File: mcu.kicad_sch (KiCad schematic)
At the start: 5 parts, among them J3 USB_C_Receptacle_USB2.0_16P, M1 Module-stlink-0.1, M3 Module-mega-mcu144-0.6

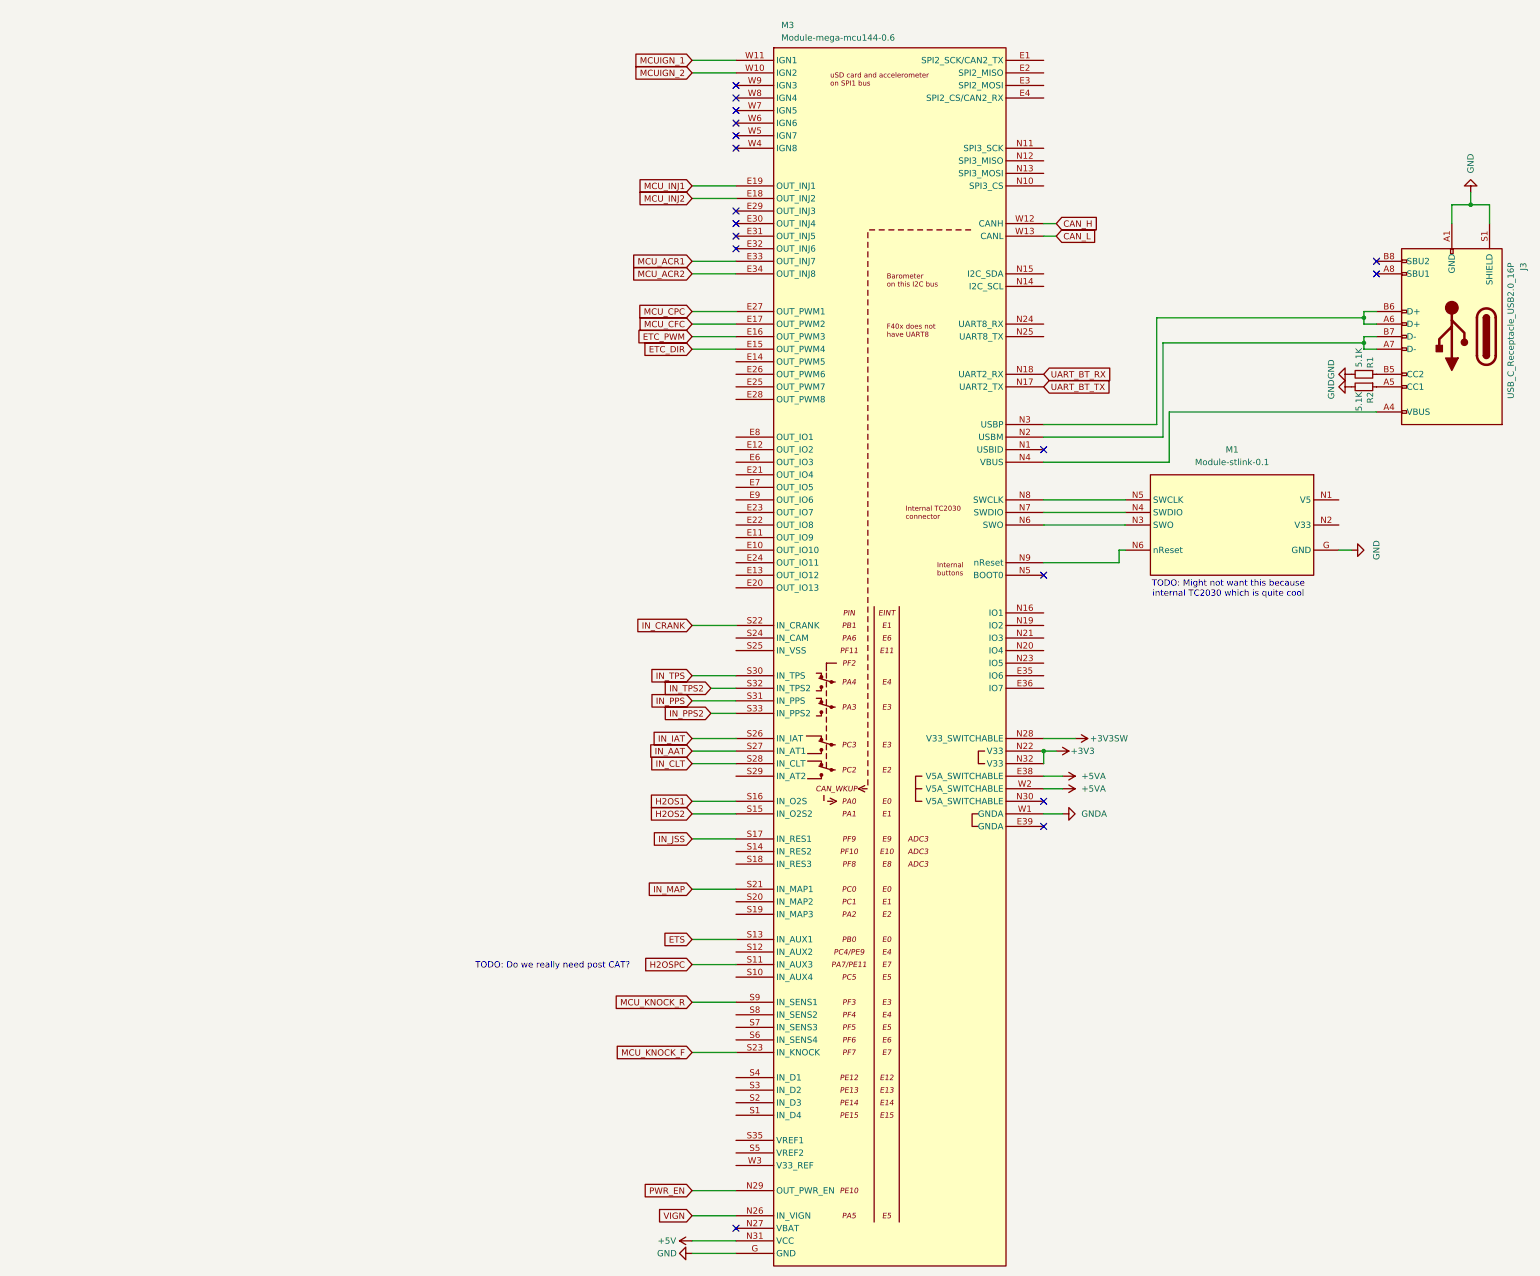
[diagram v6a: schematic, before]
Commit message: adding most remaining outputs and sensors like vvt, cam etc
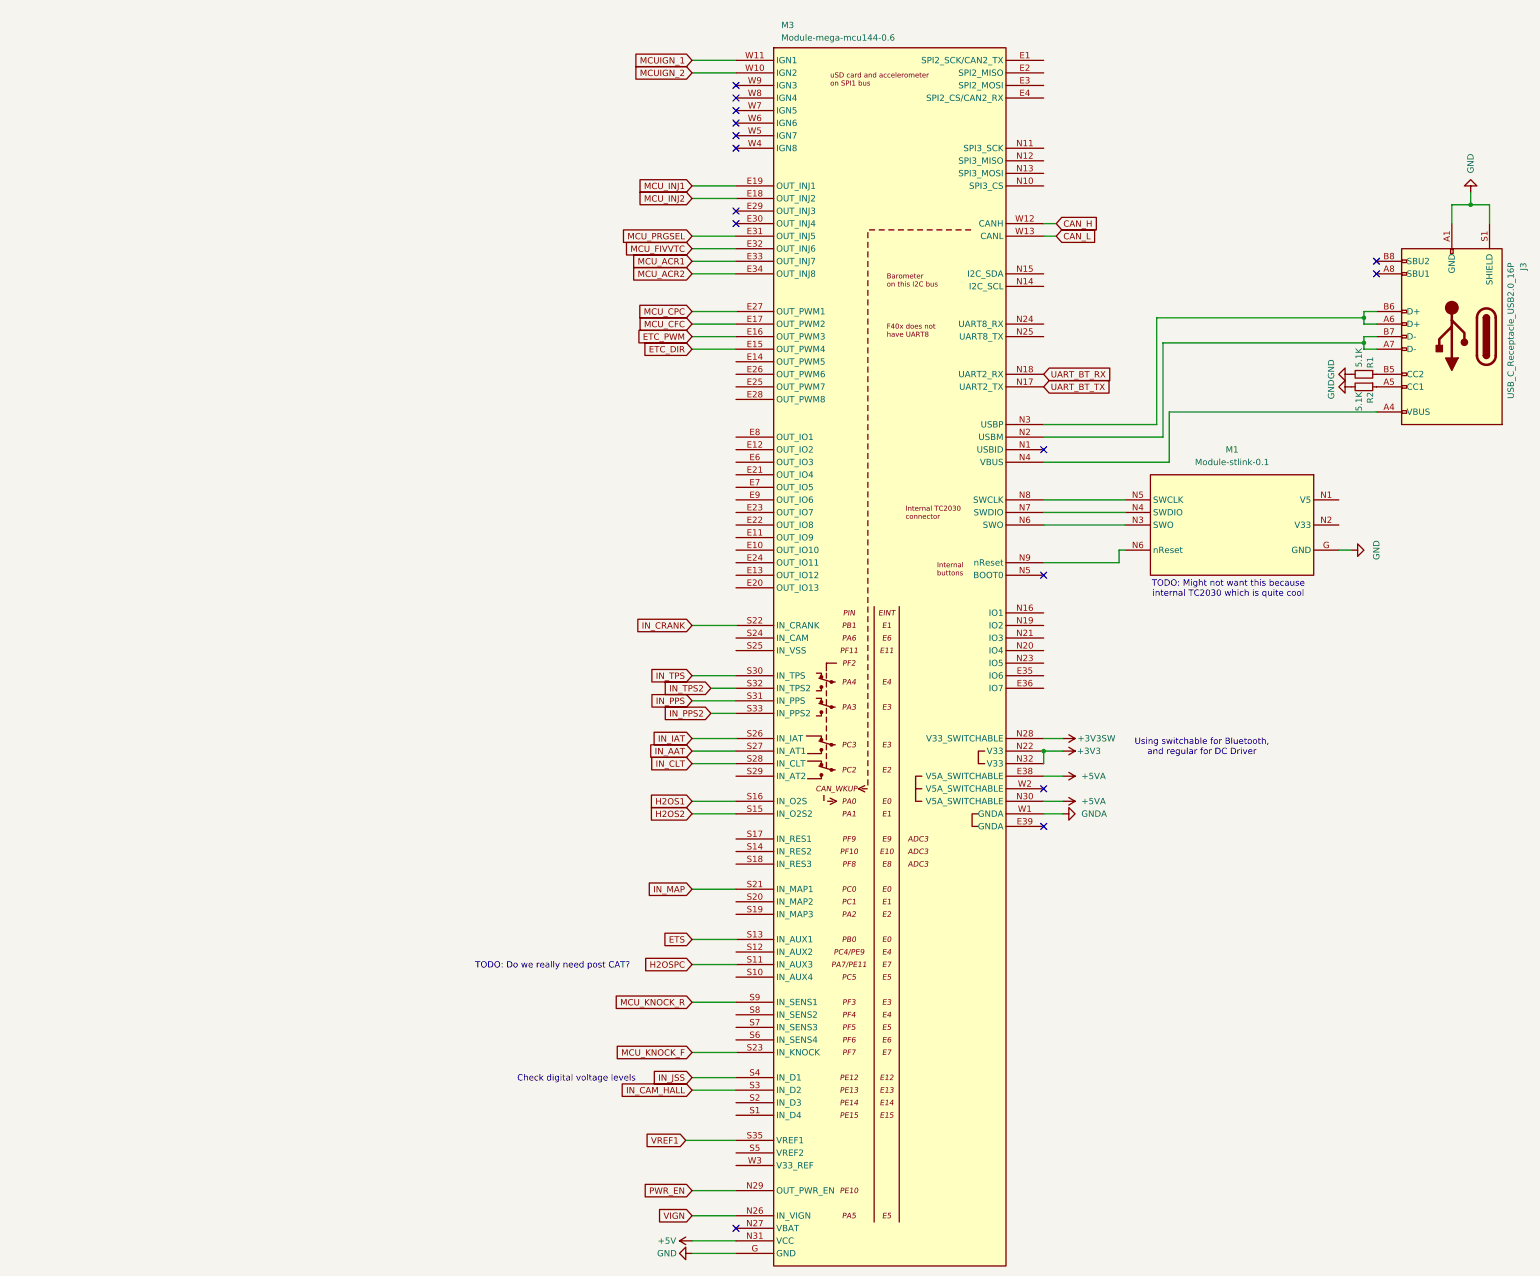
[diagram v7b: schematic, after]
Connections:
- net +5VA: now also M3.N30 (V5A_SWITCHABLE); no longer M3.W2 (V5A_SWITCHABLE)
- net IN_JSS: now also M3.S4 (IN_D1); no longer M3.S17 (IN_RES1)
- net MCU_PRGSEL: now reaches M3.E31 (OUT_INJ5)
- net MCU_FIVVTC: now reaches M3.E32 (OUT_INJ6)
- net IN_CAM_HALL: now reaches M3.S3 (IN_D2)
- net VREF1: now reaches M3.S35 (VREF1)
- no-connect marks 17 -> 15
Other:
- note added: "Check digital voltage levels"
- note added: "Using switchable for Bluetooth, and regular for DC Driver"
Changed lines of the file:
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@@
-	)
-	(no_connect
-		(at 168.91 60.96)
 	)
 	(no_connect
@@
 	)
 	(no_connect
-		(at 231.14 175.26)
-	)
-	(no_connect
 		(at 168.91 35.56)
 	)
@@
 	)
 	(no_connect
+		(at 231.14 172.72)
+	)
+	(no_connect
 		(at 168.91 38.1)
 	)
@@
 	)
 	(no_connect
-		(at 168.91 63.5)
-	)
-	(no_connect
 		(at 298.45 68.58)
 	)
@@
 	(wire
 		(pts
-			(xy 168.91 182.88) (xy 160.02 182.88)
-		)
-		(stroke
-			(width 0)
-			(type default)
-		)
-	)
-	(wire
-		(pts
 			(xy 255.27 82.55) (xy 255.27 101.6)
 		)
@@
 	(wire
 		(pts
+			(xy 158.75 243.84) (xy 168.91 243.84)
+		)
+		(stroke
+			(width 0)
+			(type default)
+		)
+	)
+	(wire
+		(pts
 			(xy 254 77.47) (xy 295.91 77.47)
 		)
@@
 	(wire
 		(pts
+			(xy 160.02 63.5) (xy 168.91 63.5)
+		)
+		(stroke
+			(width 0)
+			(type default)
+		)
+	)
+	(wire
+		(pts
 			(xy 298.45 83.82) (xy 295.91 83.82)
 		)
@@
 	(wire
 		(pts
-			(xy 233.68 165.1) (xy 231.14 165.1)
+			(xy 234.95 165.1) (xy 231.14 165.1)
+		)
+		(stroke
+			(width 0)
+			(type default)
+		)
+	)
+	(wire
+		(pts
+			(xy 168.91 231.14) (xy 160.02 231.14)
 		)
 		(stroke
@@
 	(wire
 		(pts
+			(xy 160.02 233.68) (xy 168.91 233.68)
+		)
+		(stroke
+			(width 0)
+			(type default)
+		)
+	)
+	(wire
+		(pts
 			(xy 231.14 99.06) (xy 254 99.06)
 		)
@@
 	(wire
 		(pts
+			(xy 160.02 60.96) (xy 168.91 60.96)
+		)
+		(stroke
+			(width 0)
+			(type default)
+		)
+	)
+	(wire
+		(pts
 			(xy 321.31 58.42) (xy 321.31 54.61)
 		)
@@
 	(wire
 		(pts
+			(xy 231.14 175.26) (xy 234.95 175.26)
+		)
+		(stroke
+			(width 0)
+			(type default)
+		)
+	)
+	(wire
+		(pts
 			(xy 168.91 149.86) (xy 160.02 149.86)
 		)
@@
 	(wire
 		(pts
-			(xy 237.49 162.56) (xy 231.14 162.56)
+			(xy 234.95 162.56) (xy 231.14 162.56)
 		)
 		(stroke
@@
 	(wire
 		(pts
-			(xy 231.14 172.72) (xy 234.95 172.72)
-		)
-		(stroke
-			(width 0)
-			(type default)
-		)
-	)
-	(wire
-		(pts
 			(xy 168.91 215.9) (xy 160.02 215.9)
 		)
@@
 			(width 0)
 			(type default)
+		)
+	)
+	(text "Using switchable for Bluetooth,\nand regular for DC Driver"
+		(exclude_from_sim no)
+		(at 263.144 164.338 0)
+		(effects
+			(font
+				(size 1.27 1.27)
+			)
 		)
 	)
@@
 		)
 	)
+	(text "Check digital voltage levels"
+		(exclude_from_sim no)
+		(at 136.652 231.394 0)
+		(effects
+			(font
+				(size 1.27 1.27)
+			)
+		)
+	)
 	(global_label "H2OSPC"
 		(shape input)
@@
 		)
 	)
+	(global_label "VREF1"
+		(shape input)
+		(at 158.75 243.84 180)
+		(fields_autoplaced yes)
+		(effects
+			(font
+				(size 1.27 1.27)
+			)
+			(justify right)
+		)
+		(property "Intersheetrefs" "${INTERSHEET_REFS}"
+			(at 149.9591 243.84 0)
+			(effects
+				(font
+					(size 1.27 1.27)
+				)
+				(justify right)
+				(hide yes)
+			)
+		)
+	)
 	(global_label "MCU_CPC"
 		(shape input)
@@
 		)
 	)
+	(global_label "MCU_PRGSEL"
+		(shape input)
+		(at 160.02 60.96 180)
+		(fields_autoplaced yes)
+		(effects
+			(font
+				(size 1.27 1.27)
+			)
+			(justify right)
+		)
+		(property "Intersheetrefs" "${INTERSHEET_REFS}"
+			(at 144.8187 60.96 0)
+			(effects
+				(font
+					(size 1.27 1.27)
+				)
+				(justify right)
+				(hide yes)
+			)
+		)
+	)
 	(global_label "IN_MAP"
 		(shape input)
@@
 	(global_label "IN_JSS"
 		(shape input)
-		(at 160.02 182.88 180)
-		(fields_autoplaced yes)
-		(effects
-			(font
-				(size 1.27 1.27)
-			)
-			(justify right)
-		)
-		(property "Intersheetrefs" "${INTERSHEET_REFS}"
-			(at 150.7453 182.88 0)
+		(at 160.02 231.14 180)
+		(fields_autoplaced yes)
+		(effects
+			(font
+				(size 1.27 1.27)
+			)
+			(justify right)
+		)
+		(property "Intersheetrefs" "${INTERSHEET_REFS}"
+			(at 150.7453 231.14 0)
 			(effects
 				(font
@@
 		)
 	)
+	(global_label "MCU_FIVVTC"
+		(shape input)
+		(at 160.02 63.5 180)
+		(fields_autoplaced yes)
+		(effects
+			(font
+				(size 1.27 1.27)
+			)
+			(justify right)
+		)
+		(property "Intersheetrefs" "${INTERSHEET_REFS}"
+			(at 145.9071 63.5 0)
+			(effects
+				(font
+					(size 1.27 1.27)
+				)
+				(justify right)
+				(hide yes)
+			)
+		)
+	)
 	(global_label "ETC_PWM"
 		(shape input)
@@
 		(property "Intersheetrefs" "${INTERSHEET_REFS}"
 			(at 152.7409 259.08 0)
+			(effects
+				(font
+					(size 1.27 1.27)
+				)
+				(justify right)
+				(hide yes)
+			)
+		)
+	)
+	(global_label "IN_CAM_HALL"
+		(shape input)
+		(at 160.02 233.68 180)
+		(fields_autoplaced yes)
+		(effects
+			(font
+				(size 1.27 1.27)
+			)
+			(justify right)
+		)
+		(property "Intersheetrefs" "${INTERSHEET_REFS}"
+			(at 144.879 233.68 0)
 			(effects
 				(font
@@
 	(symbol
 		(lib_id "power:+3V3")
-		(at 237.49 162.56 270)
+		(at 234.95 162.56 270)
 		(unit 1)
 		(exclude_from_sim no)
@@
 		(dnp no)
 		(property "Reference" "#PWR037"
-			(at 233.68 162.56 0)
+			(at 231.14 162.56 0)
 			(effects
 				(font
@@
 		)
 		(property "Value" "+3V3SW"
-			(at 244.348 162.56 90)
+			(at 241.808 162.56 90)
 			(effects
 				(font
@@
 		)
 		(property "Footprint" ""
-			(at 237.49 162.56 0)
+			(at 234.95 162.56 0)
 			(effects
 				(font
@@
 		)
 		(property "Datasheet" ""
-			(at 237.49 162.56 0)
+			(at 234.95 162.56 0)
 			(effects
 				(font
@@
 		)
 		(property "Description" "Power symbol creates a global label with name \"+3V3\""
-			(at 237.49 162.56 0)
+			(at 234.95 162.56 0)
 			(effects
 				(font
@@
 	(symbol
 		(lib_id "power:+3V3")
-		(at 233.68 165.1 270)
+		(at 234.95 165.1 270)
 		(unit 1)
 		(exclude_from_sim no)
@@
 		(dnp no)
 		(property "Reference" "#PWR036"
-			(at 229.87 165.1 0)
+			(at 231.14 165.1 0)
 			(effects
 				(font
@@
 		)
 		(property "Value" "+3V3"
-			(at 239.014 165.1 90)
+			(at 240.284 165.1 90)
 			(effects
 				(font
@@
 		)
 		(property "Footprint" ""
-			(at 233.68 165.1 0)
+			(at 234.95 165.1 0)
 			(effects
 				(font
@@
 		)
 		(property "Datasheet" ""
-			(at 233.68 165.1 0)
+			(at 234.95 165.1 0)
 			(effects
 				(font
@@
 		)
 		(property "Description" "Power symbol creates a global label with name \"+3V3\""
-			(at 233.68 165.1 0)
+			(at 234.95 165.1 0)
 			(effects
 				(font
@@
 	(symbol
 		(lib_id "power:+5VA")
-		(at 234.95 172.72 270)
+		(at 234.95 175.26 270)
 		(unit 1)
 		(exclude_from_sim no)
@@
 		(fields_autoplaced yes)
 		(property "Reference" "#PWR051"
-			(at 231.14 172.72 0)
+			(at 231.14 175.26 0)
 			(effects
 				(font
@@
 		)
 		(property "Value" "+5VA"
-			(at 238.76 172.7199 90)
+			(at 238.76 175.2599 90)
 			(effects
 				(font
@@
 		)
 		(property "Footprint" ""
-			(at 234.95 172.72 0)
+			(at 234.95 175.26 0)
 			(effects
 				(font
@@
 		)
 		(property "Datasheet" ""
-			(at 234.95 172.72 0)
+			(at 234.95 175.26 0)
 			(effects
 				(font
@@
 		)
 		(property "Description" "Power symbol creates a global label with name \"+5VA\""
-			(at 234.95 172.72 0)
-			(effects
-				(font
+			(at 234.95 175.26 0)
+			(effects
+				(font

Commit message: redone layout, possibly feature complete
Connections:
- net +3V3: no longer M3.N22 (V33)
- net +5VA: now also M3.W2 (V5A_SWITCHABLE); no longer M3.N30 (V5A_SWITCHABLE)
- net ETS: now also M3.S8 (IN_SENS2); no longer M3.S13 (IN_AUX1)
- net MCUIGN_1: now also M3.W10 (IGN2); no longer M3.W11 (IGN1)
- net MCUIGN_2: now also M3.W11 (IGN1); no longer M3.W10 (IGN2)
- net MCU_CCFC: now reaches M3.E14 (OUT_PWM5)
- net MCU_PCHO2SHTR: now reaches M3.E26 (OUT_PWM6)
- net MCU_FHO2H: now reaches M3.E29 (OUT_INJ3)
- net MCU_RHO2H: now reaches M3.E30 (OUT_INJ4)
- net VREF2: now reaches M3.S5 (VREF2)
- net GEAR_POS_SENS: now reaches M3.S6 (IN_SENS4)
- net FLS: now reaches M3.S7 (IN_SENS3)
- no-connect marks 15 -> 14
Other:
- note added: "Using switchable for Bluetooth, and regular 3v3 for DC Driver"
- note removed: "Using switchable for Bluetooth, and regular for DC Driver"
